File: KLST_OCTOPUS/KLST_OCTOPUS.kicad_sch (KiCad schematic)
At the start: 19 parts, among them J1 MIDI IN, J2 MIDI OUT, J3 MIDI THRU, J4 UART, U1 H11L1SR2M, U2 74AHC1G125, U3 74AHC1G125, X1 KLST_ICON

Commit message: prepared components for production
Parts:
- C1: JLCPCB Part # C696821 -> (none); LCSC (none) -> C696821; LCSC Part # C696821 -> (none); MFR.Part # T529P106M010AAE200 -> (none)
- D1: JLCPCB Part # C896167 -> (none); LCSC (none) -> C896167; LCSC Part # C896167 -> (none); MFR.Part # 1N914BWT -> (none)
- H1, H2, JP1, X1: JLCPCB Part # - -> (none)
- J1, J2, J3: JLCPCB Part # C2939344 -> (none); LCSC (none) -> C2939344; LCSC Part # C2939344 -> (none); MFR.Part # DIN-504-M10 -> (none)
- J4: JLCPCB Part # C146629 -> (none); LCSC (none) -> C146629; LCSC Part # C146629 -> (none); MFR.Part # B-3000R06P-0110 -> (none)
- R1, R2, R4, R5: JLCPCB Part # C328398 -> (none); LCSC (none) -> C328398; LCSC Part # C328398 -> (none); MFR.Part # AECR0805F47R0K9 -> (none)
- R3: JLCPCB Part # C479094 -> (none); LCSC (none) -> C479094; LCSC Part # C479094 -> (none); MFR.Part # PTFR0805B220RP9 -> (none)
- R6: JLCPCB Part # C328396 -> (none); LCSC (none) -> C328396; LCSC Part # C328396 -> (none); MFR.Part # AECR0805F470RK9 -> (none)
- U1: JLCPCB Part # C20082 -> (none); LCSC (none) -> C20082; LCSC Part # C20082 -> (none); MFR.Part # H11L1SR2M -> (none)
- U2, U3: JLCPCB Part # C7468 -> (none); LCSC (none) -> C5513; LCSC Part # C7468 -> (none); MFR.Part # SN74AHC1G125DBVR -> (none)
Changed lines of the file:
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@@
-      (effects (font (size 1.27 1.27)) hide)
-    )
-    (property "JLCPCB Part #" "-" (id 4) (at 229.87 43.18 0)
       (effects (font (size 1.27 1.27)) hide)
     )
@@
       (effects (font (size 1.27 1.27)) hide)
     )
-    (property "JLCPCB Part #" "-" (id 4) (at 201.93 71.12 0)
-      (effects (font (size 1.27 1.27)) hide)
-    )
     (pin "1")
     (pin "2")
@@
       (effects (font (size 2.54 2.54)) hide)
     )
-    (property "JLCPCB Part #" "-" (id 4) (at 231.14 21.59 0)
-      (effects (font (size 1.27 1.27)) hide)
-    )
   )
   (symbol (lib_id "power:+3V3") (at 20.32 71.12 0) (unit 1)
@@
       (effects (font (size 1.27 1.27)) hide)
     )
-    (property "JLCPCB Part #" "C328398" (id 5) (at 20.32 74.93 0)
-      (effects (font (size 1.27 1.27)) hide)
-    )
-    (property "MFR.Part #" "AECR0805F47R0K9" (id 6) (at 20.32 74.93 0)
-      (effects (font (size 1.27 1.27)) hide)
-    )
-    (property "LCSC Part #" "C328398" (id 7) (at 20.32 74.93 0)
+    (property "LCSC" "C328398" (id 7) (at 20.32 74.93 0)
       (effects (font (size 1.27 1.27)) hide)
     )
@@
       (effects (font (size 1.27 1.27)) hide)
     )
-    (property "MPN" "" (id 4) (at 52.07 33.02 0)
-      (effects (font (size 1.27 1.27)) hide)
-    )
     (property "Extended Part" "-" (id 5) (at 52.07 33.02 0)
       (effects (font (size 1.27 1.27)) hide)
     )
-    (property "JLCPCB Part #" "C896167" (id 6) (at 52.07 33.02 0)
-      (effects (font (size 1.27 1.27)) hide)
-    )
-    (property "MFR.Part #" "1N914BWT" (id 7) (at 52.07 33.02 0)
-      (effects (font (size 1.27 1.27)) hide)
-    )
-    (property "LCSC Part #" "C896167" (id 8) (at 52.07 33.02 0)
+    (property "LCSC" "C896167" (id 8) (at 52.07 33.02 0)
       (effects (font (size 1.27 1.27)) hide)
     )
@@
       (effects (font (size 1.27 1.27)) hide)
     )
-    (property "MFR.Part #" "B-3000R06P-0110" (id 4) (at 162.56 34.29 0)
-      (effects (font (size 1.27 1.27)) hide)
-    )
-    (property "LCSC Part #" "C146629" (id 5) (at 162.56 34.29 0)
+    (property "LCSC" "C146629" (id 5) (at 162.56 34.29 0)
       (effects (font (size 1.27 1.27)) hide)
     )
     (property "Extended Part" "-" (id 6) (at 162.56 34.29 0)
-      (effects (font (size 1.27 1.27)) hide)
-    )
-    (property "JLCPCB Part #" "C146629" (id 7) (at 162.56 34.29 0)
       (effects (font (size 1.27 1.27)) hide)
     )
@@
   )
   (symbol (lib_id "KLST-ICON:LOGO") (at 226.06 21.59 0) (unit 1)
-    (in_bom yes) (on_board yes) (fields_autoplaced)
+    (in_bom no) (on_board yes) (fields_autoplaced)
     (property "Reference" "#G1" (id 0) (at 226.06 28.4734 0)
       (effects (font (size 1.524 1.524)) hide)
     )
-    (property "Value" "LOGO" (id 1) (at 226.06 14.7066 0)
+    (property "Value" "" (id 1) (at 226.06 14.7066 0)
       (effects (font (size 1.524 1.524)) hide)
     )
@@
       (effects (font (size 1.27 1.27)) hide)
     )
-    (property "JLCPCB Part #" "C328398" (id 5) (at 20.32 128.27 0)
-      (effects (font (size 1.27 1.27)) hide)
-    )
-    (property "MFR.Part #" "AECR0805F47R0K9" (id 6) (at 20.32 128.27 0)
-      (effects (font (size 1.27 1.27)) hide)
-    )
-    (property "LCSC Part #" "C328398" (id 7) (at 20.32 128.27 0)
+    (property "LCSC" "C328398" (id 7) (at 20.32 128.27 0)
       (effects (font (size 1.27 1.27)) hide)
     )
@@
       (effects (font (size 1.27 1.27)) hide)
     )
-    (property "JLCPCB Part #" "C7468" (id 5) (at 81.28 85.09 0)
-      (effects (font (size 1.27 1.27)) hide)
-    )
-    (property "MFR.Part #" "SN74AHC1G125DBVR" (id 6) (at 81.28 85.09 0)
-      (effects (font (size 1.27 1.27)) hide)
-    )
-    (property "LCSC Part #" "C7468" (id 7) (at 81.28 85.09 0)
+    (property "LCSC" "C5513" (id 7) (at 81.28 85.09 0)
       (effects (font (size 1.27 1.27)) hide)
     )
@@
       (effects (font (size 1.27 1.27)) hide)
     )
-    (property "MPN" "" (id 4) (at 29.21 87.63 0)
-      (effects (font (size 1.27 1.27)) hide)
-    )
     (property "Extended Part" "-" (id 5) (at 29.21 87.63 0)
       (effects (font (size 1.27 1.27)) hide)
     )
-    (property "JLCPCB Part #" "C2939344" (id 6) (at 29.21 87.63 0)
-      (effects (font (size 1.27 1.27)) hide)
-    )
-    (property "MFR.Part #" "DIN-504-M10" (id 7) (at 29.21 87.63 0)
-      (effects (font (size 1.27 1.27)) hide)
-    )
-    (property "LCSC Part #" "C2939344" (id 8) (at 29.21 87.63 0)
+    (property "LCSC" "C2939344" (id 8) (at 29.21 87.63 0)
       (effects (font (size 1.27 1.27)) hide)
     )
@@
       (effects (font (size 1.27 1.27)) hide)
     )
-    (property "JLCPCB Part #" "C20082" (id 4) (at 67.31 35.56 0)
-      (effects (font (size 1.27 1.27)) hide)
-    )
     (property "Extended Part" "-" (id 5) (at 67.31 35.56 0)
       (effects (font (size 1.27 1.27)) hide)
     )
-    (property "MFR.Part #" "H11L1SR2M" (id 6) (at 67.31 35.56 0)
-      (effects (font (size 1.27 1.27)) hide)
-    )
-    (property "LCSC Part #" "C20082" (id 7) (at 67.31 35.56 0)
+    (property "LCSC" "C20082" (id 7) (at 67.31 35.56 0)
       (effects (font (size 1.27 1.27)) hide)
     )
@@
       (effects (font (size 1.27 1.27)) hide)
     )
-    (property "JLCPCB Part #" "C7468" (id 5) (at 81.28 138.43 0)
-      (effects (font (size 1.27 1.27)) hide)
-    )
-    (property "MFR.Part #" "SN74AHC1G125DBVR" (id 6) (at 81.28 138.43 0)
-      (effects (font (size 1.27 1.27)) hide)
-    )
-    (property "LCSC Part #" "C7468" (id 7) (at 81.28 138.43 0)
+    (property "LCSC" "C5513" (id 7) (at 81.28 138.43 0)
       (effects (font (size 1.27 1.27)) hide)
     )
@@
       (effects (font (size 1.27 1.27)) hide)
     )
-    (property "MPN" "" (id 4) (at 25.4 40.64 0)
-      (effects (font (size 1.27 1.27)) hide)
-    )
     (property "Extended Part" "-" (id 5) (at 25.4 40.64 0)
       (effects (font (size 1.27 1.27)) hide)
     )
-    (property "JLCPCB Part #" "C2939344" (id 6) (at 25.4 40.64 0)
-      (effects (font (size 1.27 1.27)) hide)
-    )
-    (property "MFR.Part #" "DIN-504-M10" (id 7) (at 25.4 40.64 0)
-      (effects (font (size 1.27 1.27)) hide)
-    )
-    (property "LCSC Part #" "C2939344" (id 8) (at 25.4 40.64 0)
+    (property "LCSC" "C2939344" (id 8) (at 25.4 40.64 0)
       (effects (font (size 1.27 1.27)) hide)
     )
@@
       (effects (font (size 1.27 1.27)) hide)
     )
-    (property "JLCPCB Part #" "C328398" (id 5) (at 41.91 138.43 0)
-      (effects (font (size 1.27 1.27)) hide)
-    )
-    (property "MFR.Part #" "AECR0805F47R0K9" (id 6) (at 41.91 138.43 0)
-      (effects (font (size 1.27 1.27)) hide)
-    )
-    (property "LCSC Part #" "C328398" (id 7) (at 41.91 138.43 0)
+    (property "LCSC" "C328398" (id 7) (at 41.91 138.43 0)
       (effects (font (size 1.27 1.27)) hide)
     )
@@
       (effects (font (size 1.27 1.27)) hide)
     )
-    (property "JLCPCB Part #" "C479094" (id 5) (at 40.64 27.94 0)
-      (effects (font (size 1.27 1.27)) hide)
-    )
-    (property "MFR.Part #" "PTFR0805B220RP9" (id 6) (at 40.64 27.94 0)
-      (effects (font (size 1.27 1.27)) hide)
-    )
-    (property "LCSC Part #" "C479094" (id 7) (at 40.64 27.94 0)
+    (property "LCSC" "C479094" (id 7) (at 40.64 27.94 0)
       (effects (font (size 1.27 1.27)) hide)
     )
@@
       (effects (font (size 1.27 1.27)) hide)
     )
-    (property "MPN" "" (id 4) (at 99.06 34.29 0)
-      (effects (font (size 1.27 1.27)) hide)
-    )
     (property "Extended Part" "-" (id 5) (at 99.06 34.29 0)
       (effects (font (size 1.27 1.27)) hide)
     )
-    (property "JLCPCB Part #" "C696821" (id 6) (at 99.06 34.29 0)
-      (effects (font (size 1.27 1.27)) hide)
-    )
-    (property "MFR.Part #" "T529P106M010AAE200" (id 7) (at 99.06 34.29 0)
-      (effects (font (size 1.27 1.27)) hide)
-    )
-    (property "LCSC Part #" "C696821" (id 8) (at 99.06 34.29 0)
+    (property "LCSC" "C696821" (id 8) (at 99.06 34.29 0)
       (effects (font (size 1.27 1.27)) hide)
     )
@@
     )
     (property "Datasheet" "~" (id 3) (at 229.87 35.56 0)
-      (effects (font (size 1.27 1.27)) hide)
-    )
-    (property "JLCPCB Part #" "-" (id 4) (at 229.87 35.56 0)
       (effects (font (size 1.27 1.27)) hide)
     )
@@
       (effects (font (size 1.27 1.27)) hide)
     )
-    (property "MPN" "" (id 4) (at 29.21 140.97 0)
-      (effects (font (size 1.27 1.27)) hide)
-    )
     (property "Extended Part" "-" (id 5) (at 29.21 140.97 0)
       (effects (font (size 1.27 1.27)) hide)
     )
-    (property "JLCPCB Part #" "C2939344" (id 6) (at 29.21 140.97 0)
-      (effects (font (size 1.27 1.27)) hide)
-    )
-    (property "MFR.Part #" "DIN-504-M10" (id 7) (at 29.21 140.97 0)
-      (effects (font (size 1.27 1.27)) hide)
-    )
-    (property "LCSC Part #" "C2939344" (id 8) (at 29.21 140.97 0)
+    (property "LCSC" "C2939344" (id 8) (at 29.21 140.97 0)
       (effects (font (size 1.27 1.27)) hide)
     )
@@
       (effects (font (size 1.27 1.27)) hide)
     )
-    (property "JLCPCB Part #" "C328396" (id 5) (at 77.47 30.48 0)
-      (effects (font (size 1.27 1.27)) hide)
-    )
-    (property "MFR.Part #" "AECR0805F470RK9" (id 6) (at 77.47 30.48 0)
-      (effects (font (size 1.27 1.27)) hide)
-    )
-    (property "LCSC Part #" "C328396" (id 7) (at 77.47 30.48 0)
+    (property "LCSC" "C328396" (id 7) (at 77.47 30.48 0)
       (effects (font (size 1.27 1.27)) hide)
     )
@@
       (effects (font (size 1.27 1.27)) hide)
     )
-    (property "JLCPCB Part #" "C328398" (id 5) (at 41.91 85.09 0)
-      (effects (font (size 1.27 1.27)) hide)
-    )
-    (property "MFR.Part #" "AECR0805F47R0K9" (id 6) (at 41.91 85.09 0)
-      (effects (font (size 1.27 1.27)) hide)
-    )
-    (property "LCSC Part #" "C328398" (id 7) (at 41.91 85.09 0)
-      (effects (font (size 1.27 1.27)) hide)
-    )
+    (property "LCSC" "C328398" (id 7) (at 41.91 85.09 0)
+      (effects (font (size 1.27 1.27)) hide)
+    )

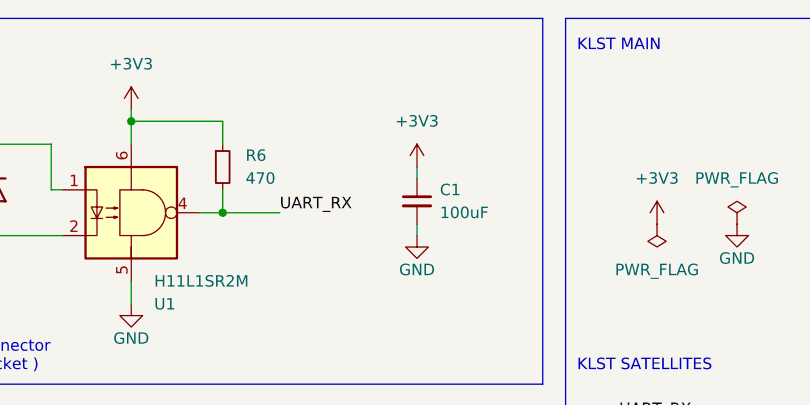
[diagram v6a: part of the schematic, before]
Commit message: corrected C1 ( to 100nF )
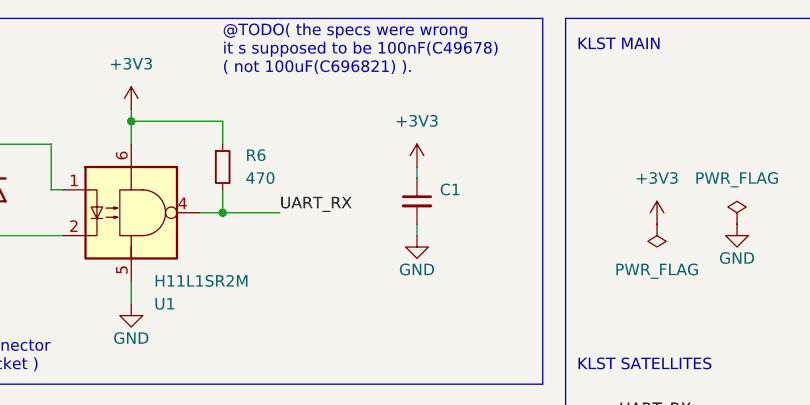
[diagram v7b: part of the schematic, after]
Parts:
- C1: value 100uF -> (none); footprint Capacitor_SMD:C_0805_2012Metric_Pad1.18x1.45mm_HandSolder -> (none); LCSC C696821 -> C49678
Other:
- note added: "@TODO( the specs were wrong it s supposed to be 100nF(C49678) ( not 100uF(C696821) )."
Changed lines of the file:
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@@
+    (effects (font (size 1.27 1.27)) (justify left bottom))
+  )
+  (text "@TODO( the specs were wrong \nit s supposed to be 100nF(C49678) \n( not 100uF(C696821) )."
+    (at 77.47 20.32 0)
     (effects (font (size 1.27 1.27)) (justify left bottom))
   )
@@
       (effects (font (size 1.524 1.524)) hide)
     )
-    (property "Value" "" (id 1) (at 226.06 14.7066 0)
+    (property "Value" "LOGO" (id 1) (at 226.06 14.7066 0)
       (effects (font (size 1.524 1.524)) hide)
     )
@@
       (effects (font (size 1.27 1.27)) (justify left))
     )
-    (property "Value" "100uF" (id 1) (at 101.6 35.5662 0)
-      (effects (font (size 1.27 1.27)) (justify left))
-    )
-    (property "Footprint" "Capacitor_SMD:C_0805_2012Metric_Pad1.18x1.45mm_HandSolder" (id 2) (at 99.06 34.29 0)
+    (property "Value" "" (id 1) (at 101.6 35.5662 0)
+      (effects (font (size 1.27 1.27)) (justify left))
+    )
+    (property "Footprint" "" (id 2) (at 99.06 34.29 0)
       (effects (font (size 1.27 1.27)) hide)
     )
@@
       (effects (font (size 1.27 1.27)) hide)
     )
-    (property "LCSC" "C696821" (id 8) (at 99.06 34.29 0)
+    (property "LCSC" "C49678 " (id 8) (at 99.06 34.29 0)
       (effects (font (size 1.27 1.27)) hide)
     )
@@
     )
     (path "/cb3a7944-5030-45f6-bc64-1e4d951d71de"
-      (reference "C1") (unit 1) (value "100uF") (footprint "Capacitor_SMD:C_0805_2012Metric_Pad1.18x1.45mm_HandSolder")
+      (reference "C1") (unit 1) (value "100nF") (footprint "Capacitor_SMD:C_0805_2012Metric_Pad1.18x1.45mm_HandSolder")
     )
     (path "/3a1d3393-5196-40a6-9b18-ab90a7f47e1f"
